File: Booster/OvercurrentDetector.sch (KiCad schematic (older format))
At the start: 35 parts, among them U202 LM339, U501 LM338, U502 LM358, U503 NE555

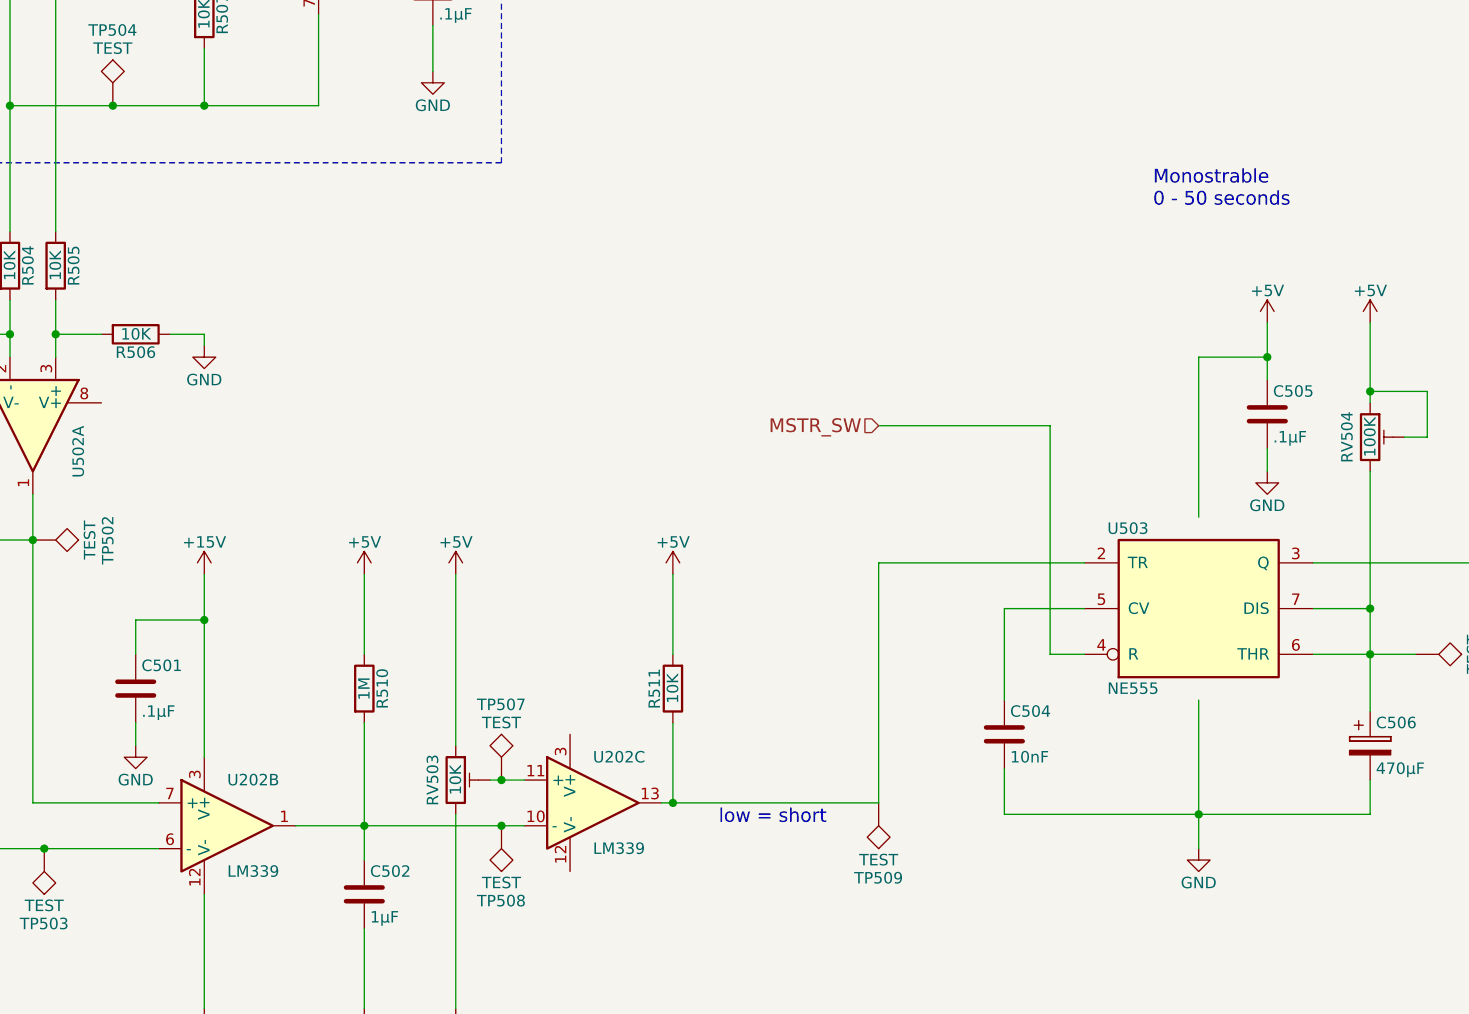
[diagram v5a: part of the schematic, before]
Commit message: Pulse detector circuit included.
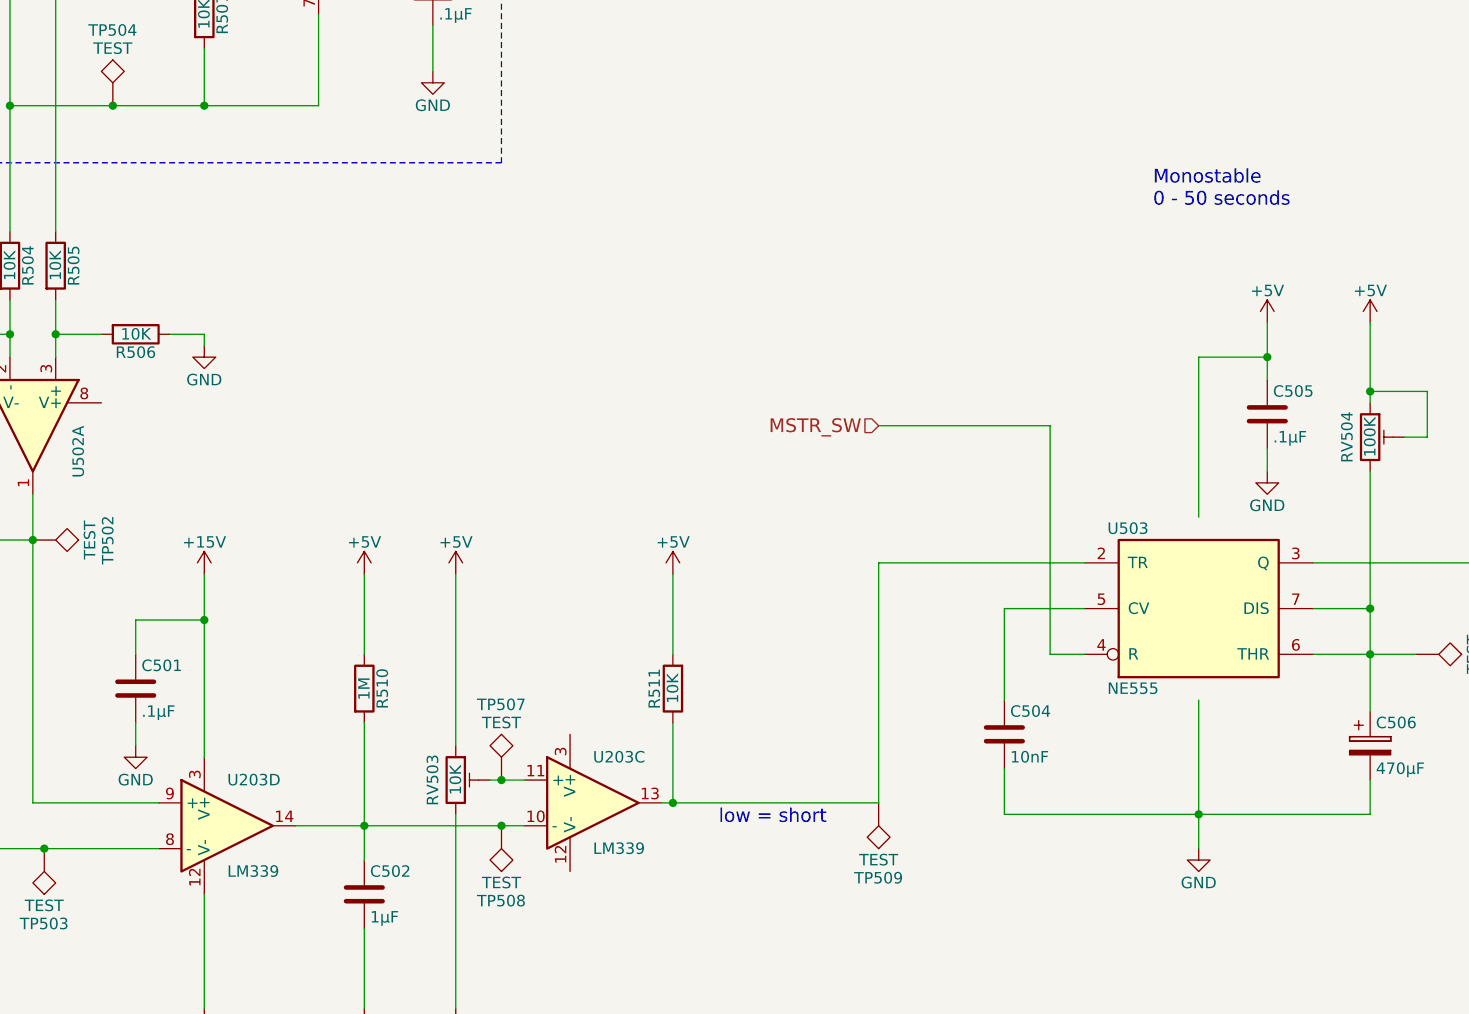
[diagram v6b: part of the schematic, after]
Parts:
- renumbered U202 to U203
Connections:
- net at R501.1, R502.2, TP503.1: now also U203.8 (-); no longer U203.6 (-)
- net at R503.2, TP502.1, U502.1: now also U203.9 (+); no longer U203.7 (+)
- net at C502.1, R510.2, TP508.1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: now also U203.14; no longer U203.1
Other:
- note added: "Monostable\n0 - 50 seconds"
- note removed: "Monostrable\n0 - 50 seconds"
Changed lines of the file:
@@
 $EndComp
 $Comp
-L GND #PWR016
+L GND #PWR501
 U 1 1 59ECCA64
 P 2500 7100
-F 0 "#PWR016" H 2500 6850 50  0001 C CNN
+F 0 "#PWR501" H 2500 6850 50  0001 C CNN
 F 1 "GND" H 2500 6950 50  0000 C CNN
 F 2 "" H 2500 7100 50  0000 C CNN
@@
 $EndComp
 $Comp
-L GND #PWR017
+L GND #PWR508
 U 1 1 5A073D4C
 P 4050 2150
-F 0 "#PWR017" H 4050 1900 50  0001 C CNN
+F 0 "#PWR508" H 4050 1900 50  0001 C CNN
 F 1 "GND" H 4050 2000 50  0000 C CNN
 F 2 "" H 4050 2150 50  0000 C CNN
@@
 $EndComp
 $Comp
-L GND #PWR018
+L GND #PWR512
 U 1 1 5A074775
 P 4900 2750
-F 0 "#PWR018" H 4900 2500 50  0001 C CNN
+F 0 "#PWR512" H 4900 2500 50  0001 C CNN
 F 1 "GND" H 4900 2600 50  0000 C CNN
 F 2 "" H 4900 2750 50  0000 C CNN
@@
 $EndComp
 $Comp
-L GND #PWR019
+L GND #PWR505
 U 1 1 5A076EC5
 P 3900 3950
-F 0 "#PWR019" H 3900 3700 50  0001 C CNN
+F 0 "#PWR505" H 3900 3700 50  0001 C CNN
 F 1 "GND" H 3900 3800 50  0000 C CNN
 F 2 "" H 3900 3950 50  0000 C CNN
@@
 $EndComp
 $Comp
-L +5V #PWR020
+L +5V #PWR503
 U 1 1 5A081F18
 P 2650 5450
-F 0 "#PWR020" H 2650 5300 50  0001 C CNN
+F 0 "#PWR503" H 2650 5300 50  0001 C CNN
 F 1 "+5V" H 2650 5590 50  0000 C CNN
 F 2 "" H 2650 5450 50  0000 C CNN
@@
 $EndComp
 $Comp
-L LM339 U202
-U 2 1 5A08213B
+L LM339 U203
+U 4 1 5A08213B
 P 4000 6050
-F 0 "U202" H 4000 6250 50  0000 L CNN
+F 0 "U203" H 4000 6250 50  0000 L CNN
 F 1 "LM339" H 4000 5850 50  0000 L CNN
 F 2 "" H 3950 6150 50  0000 C CNN
 F 3 "" H 4050 6250 50  0000 C CNN
-	2    4000 6050
+	4    4000 6050
 	1    0    0    -1
 $EndComp
@@
 $EndComp
 $Comp
-L LM339 U202
+L LM339 U203
 U 3 1 5A088F76
 P 5600 5950
-F 0 "U202" H 5600 6150 50  0000 L CNN
+F 0 "U203" H 5600 6150 50  0000 L CNN
 F 1 "LM339" H 5600 5750 50  0000 L CNN
 F 2 "" H 5550 6050 50  0000 C CNN
@@
 $EndComp
 $Comp
-L GND #PWR021
+L GND #PWR504
 U 1 1 5A092416
 P 3600 5700
-F 0 "#PWR021" H 3600 5450 50  0001 C CNN
+F 0 "#PWR504" H 3600 5450 50  0001 C CNN
 F 1 "GND" H 3600 5550 50  0000 C CNN
 F 2 "" H 3600 5700 50  0000 C CNN
@@
 $EndComp
 $Comp
-L +5V #PWR022
+L +5V #PWR509
 U 1 1 5A092870
 P 4600 4950
-F 0 "#PWR022" H 4600 4800 50  0001 C CNN
+F 0 "#PWR509" H 4600 4800 50  0001 C CNN
 F 1 "+5V" H 4600 5090 50  0000 C CNN
 F 2 "" H 4600 4950 50  0000 C CNN
@@
 $EndComp
 $Comp
-L +5V #PWR023
+L +5V #PWR513
 U 1 1 5A092928
 P 5000 4950
-F 0 "#PWR023" H 5000 4800 50  0001 C CNN
+F 0 "#PWR513" H 5000 4800 50  0001 C CNN
 F 1 "+5V" H 5000 5090 50  0000 C CNN
 F 2 "" H 5000 4950 50  0000 C CNN
@@
 $EndComp
 $Comp
-L GND #PWR024
+L GND #PWR507
 U 1 1 5A0931C8
 P 3900 6850
-F 0 "#PWR024" H 3900 6600 50  0001 C CNN
+F 0 "#PWR507" H 3900 6600 50  0001 C CNN
 F 1 "GND" H 3900 6700 50  0000 C CNN
 F 2 "" H 3900 6850 50  0000 C CNN
@@
 $EndComp
 $Comp
-L GND #PWR025
+L GND #PWR510
 U 1 1 5A093221
 P 4600 6850
-F 0 "#PWR025" H 4600 6600 50  0001 C CNN
+F 0 "#PWR510" H 4600 6600 50  0001 C CNN
 F 1 "GND" H 4600 6700 50  0000 C CNN
 F 2 "" H 4600 6850 50  0000 C CNN
@@
 $EndComp
 $Comp
-L GND #PWR026
+L GND #PWR514
 U 1 1 5A09327A
 P 5000 6850
-F 0 "#PWR026" H 5000 6600 50  0001 C CNN
+F 0 "#PWR514" H 5000 6600 50  0001 C CNN
 F 1 "GND" H 5000 6700 50  0000 C CNN
 F 2 "" H 5000 6850 50  0000 C CNN
@@
 $EndComp
 $Comp
-L +15V #PWR027
+L +15V #PWR502
 U 1 1 5A093E23
 P 2600 1200
-F 0 "#PWR027" H 2600 1050 50  0001 C CNN
+F 0 "#PWR502" H 2600 1050 50  0001 C CNN
 F 1 "+15V" H 2600 1340 50  0000 C CNN
 F 2 "" H 2600 1200 50  0000 C CNN
@@
 $EndComp
 $Comp
-L +15V #PWR028
+L +15V #PWR506
 U 1 1 5A094178
 P 3900 4950
-F 0 "#PWR028" H 3900 4800 50  0001 C CNN
+F 0 "#PWR506" H 3900 4800 50  0001 C CNN
 F 1 "+15V" H 3900 5090 50  0000 C CNN
 F 2 "" H 3900 4950 50  0000 C CNN
@@
 $EndComp
 $Comp
-L +15V #PWR029
+L +15V #PWR511
 U 1 1 5A0943E3
 P 4900 1850
-F 0 "#PWR029" H 4900 1700 50  0001 C CNN
+F 0 "#PWR511" H 4900 1700 50  0001 C CNN
 F 1 "+15V" H 4900 1990 50  0000 C CNN
 F 2 "" H 4900 1850 50  0000 C CNN
@@
 $EndComp
 $Comp
-L +5V #PWR030
+L +5V #PWR515
 U 1 1 5A36B721
 P 5950 4950
-F 0 "#PWR030" H 5950 4800 50  0001 C CNN
+F 0 "#PWR515" H 5950 4800 50  0001 C CNN
 F 1 "+5V" H 5950 5090 50  0000 C CNN
 F 2 "" H 5950 4950 50  0000 C CNN
@@
 $EndComp
 $Comp
-L +5V #PWR031
+L +5V #PWR517
 U 1 1 5A36C438
 P 8550 3850
-F 0 "#PWR031" H 8550 3700 50  0001 C CNN
+F 0 "#PWR517" H 8550 3700 50  0001 C CNN
 F 1 "+5V" H 8550 3990 50  0000 C CNN
 F 2 "" H 8550 3850 50  0000 C CNN
@@
 $EndComp
 $Comp
-L GND #PWR032
+L GND #PWR518
 U 1 1 5A36CF5F
 P 8550 4500
-F 0 "#PWR032" H 8550 4250 50  0001 C CNN
+F 0 "#PWR518" H 8550 4250 50  0001 C CNN
 F 1 "GND" H 8550 4350 50  0000 C CNN
 F 2 "" H 8550 4500 50  0000 C CNN
@@
 $EndComp
 $Comp
-L +5V #PWR033
+L +5V #PWR519
 U 1 1 5A36D304
 P 9000 3850
-F 0 "#PWR033" H 9000 3700 50  0001 C CNN
+F 0 "#PWR519" H 9000 3700 50  0001 C CNN
 F 1 "+5V" H 9000 3990 50  0000 C CNN
 F 2 "" H 9000 3850 50  0000 C CNN
@@
 Connection ~ 8250 6000
 $Comp
-L GND #PWR034
+L GND #PWR516
 U 1 1 5A36DC1B
 P 8250 6150
-F 0 "#PWR034" H 8250 5900 50  0001 C CNN
+F 0 "#PWR516" H 8250 5900 50  0001 C CNN
 F 1 "GND" H 8250 6000 50  0000 C CNN
 F 2 "" H 8250 6150 50  0000 C CNN
@@
 	9000 6000 9000 5850
 Text Notes 8050 3350 0    60   ~ 0
-Monostrable\n0 - 50 seconds
+Monostable\n0 - 50 seconds
 $Comp
 L TEST TP509

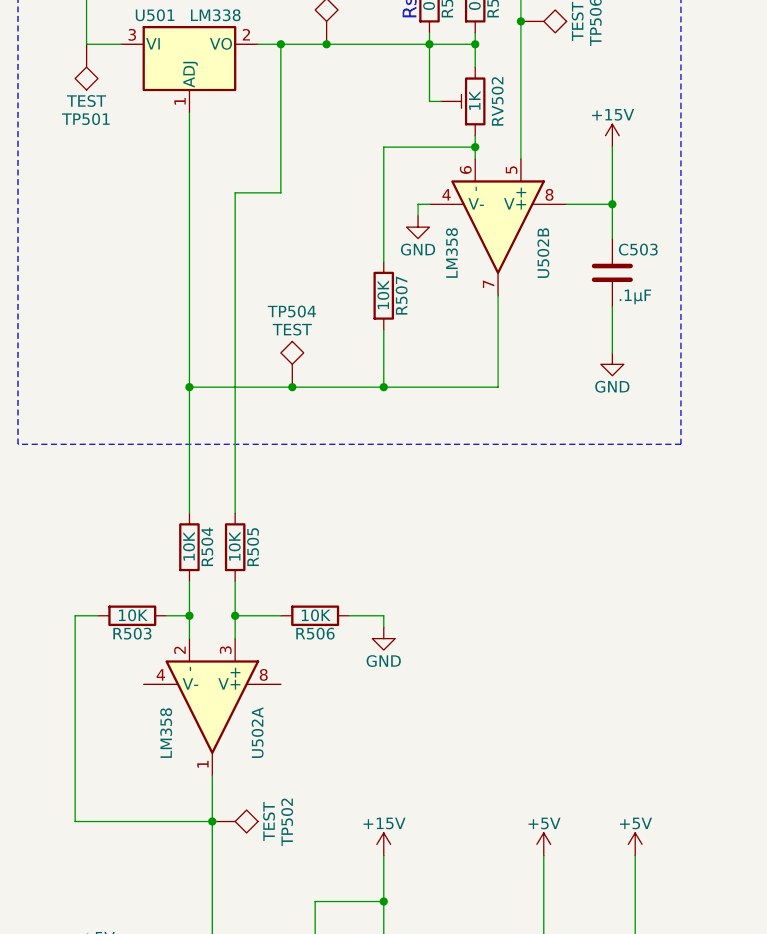
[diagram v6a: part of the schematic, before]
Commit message: Various adjustments based on breadboard prototype.
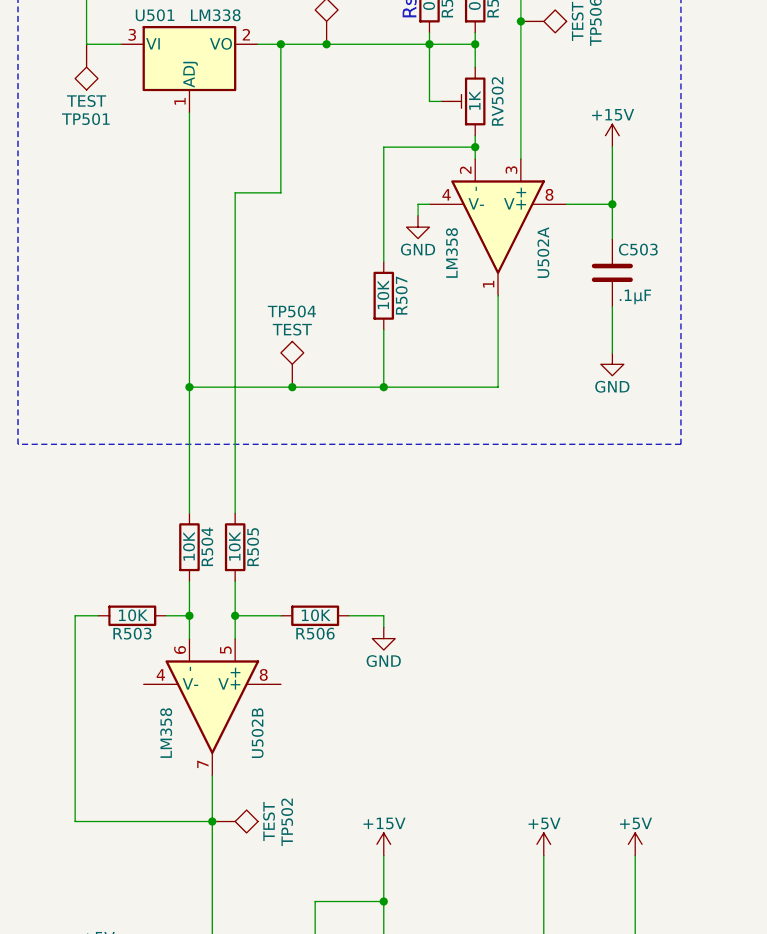
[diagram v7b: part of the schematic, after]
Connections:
- net VCC_DRIVER: now also U502.3 (+); no longer U502.5 (+)
- net at R504.1, R507.2, TP504.1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: now also U502.1; no longer U502.7
- net at R507.1, RV502.1: now also U502.2 (-); no longer U502.6 (-)
- net at R503.2, TP502.1, U203.9 (+): now also U502.7; no longer U502.1
- net at R503.1, R504.2: now also U502.6 (-); no longer U502.2 (-)
- net at R505.2, R506.2: now also U502.5 (+); no longer U502.3 (+)
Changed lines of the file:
@@
 $EndComp
 $Comp
-L GND #PWR501
+L GND #PWR019
 U 1 1 59ECCA64
 P 2500 7100
-F 0 "#PWR501" H 2500 6850 50  0001 C CNN
+F 0 "#PWR019" H 2500 6850 50  0001 C CNN
 F 1 "GND" H 2500 6950 50  0000 C CNN
 F 2 "" H 2500 7100 50  0000 C CNN
@@
 $Comp
 L LM358 U502
-U 2 1 5A071933
+U 1 1 5A071933
 P 4400 2200
 F 0 "U502" H 4400 2400 50  0000 L CNN
@@
 F 2 "" H 4400 2200 50  0001 C CNN
 F 3 "" H 4400 2200 50  0001 C CNN
-	2    4400 2200
+	1    4400 2200
 	0    1    1    0
 $EndComp
@@
 $EndComp
 $Comp
-L GND #PWR508
+L GND #PWR020
 U 1 1 5A073D4C
 P 4050 2150
-F 0 "#PWR508" H 4050 1900 50  0001 C CNN
+F 0 "#PWR020" H 4050 1900 50  0001 C CNN
 F 1 "GND" H 4050 2000 50  0000 C CNN
 F 2 "" H 4050 2150 50  0000 C CNN
@@
 $EndComp
 $Comp
-L GND #PWR512
+L GND #PWR021
 U 1 1 5A074775
 P 4900 2750
-F 0 "#PWR512" H 4900 2500 50  0001 C CNN
+F 0 "#PWR021" H 4900 2500 50  0001 C CNN
 F 1 "GND" H 4900 2600 50  0000 C CNN
 F 2 "" H 4900 2750 50  0000 C CNN
@@
 $Comp
 L LM358 U502
-U 1 1 5A076258
+U 2 1 5A076258
 P 3150 4300
 F 0 "U502" H 3150 4500 50  0000 L CNN
@@
 F 2 "" H 3150 4300 50  0001 C CNN
 F 3 "" H 3150 4300 50  0001 C CNN
-	1    3150 4300
+	2    3150 4300
 	0    1    1    0
 $EndComp
@@
 $EndComp
 $Comp
-L GND #PWR505
+L GND #PWR022
 U 1 1 5A076EC5
 P 3900 3950
-F 0 "#PWR505" H 3900 3700 50  0001 C CNN
+F 0 "#PWR022" H 3900 3700 50  0001 C CNN
 F 1 "GND" H 3900 3800 50  0000 C CNN
 F 2 "" H 3900 3950 50  0000 C CNN
@@
 $EndComp
 $Comp
-L +5V #PWR503
+L +5V #PWR023
 U 1 1 5A081F18
 P 2650 5450
-F 0 "#PWR503" H 2650 5300 50  0001 C CNN
+F 0 "#PWR023" H 2650 5300 50  0001 C CNN
 F 1 "+5V" H 2650 5590 50  0000 C CNN
 F 2 "" H 2650 5450 50  0000 C CNN
@@
 $EndComp
 $Comp
-L GND #PWR504
+L GND #PWR024
 U 1 1 5A092416
 P 3600 5700
-F 0 "#PWR504" H 3600 5450 50  0001 C CNN
+F 0 "#PWR024" H 3600 5450 50  0001 C CNN
 F 1 "GND" H 3600 5550 50  0000 C CNN
 F 2 "" H 3600 5700 50  0000 C CNN
@@
 $EndComp
 $Comp
-L +5V #PWR509
+L +5V #PWR025
 U 1 1 5A092870
 P 4600 4950
-F 0 "#PWR509" H 4600 4800 50  0001 C CNN
+F 0 "#PWR025" H 4600 4800 50  0001 C CNN
 F 1 "+5V" H 4600 5090 50  0000 C CNN
 F 2 "" H 4600 4950 50  0000 C CNN
@@
 $EndComp
 $Comp
-L +5V #PWR513
+L +5V #PWR026
 U 1 1 5A092928
 P 5000 4950
-F 0 "#PWR513" H 5000 4800 50  0001 C CNN
+F 0 "#PWR026" H 5000 4800 50  0001 C CNN
 F 1 "+5V" H 5000 5090 50  0000 C CNN
 F 2 "" H 5000 4950 50  0000 C CNN
@@
 $EndComp
 $Comp
-L GND #PWR507
+L GND #PWR027
 U 1 1 5A0931C8
 P 3900 6850
-F 0 "#PWR507" H 3900 6600 50  0001 C CNN
+F 0 "#PWR027" H 3900 6600 50  0001 C CNN
 F 1 "GND" H 3900 6700 50  0000 C CNN
 F 2 "" H 3900 6850 50  0000 C CNN
@@
 $EndComp
 $Comp
-L GND #PWR510
+L GND #PWR028
 U 1 1 5A093221
 P 4600 6850
-F 0 "#PWR510" H 4600 6600 50  0001 C CNN
+F 0 "#PWR028" H 4600 6600 50  0001 C CNN
 F 1 "GND" H 4600 6700 50  0000 C CNN
 F 2 "" H 4600 6850 50  0000 C CNN
@@
 $EndComp
 $Comp
-L GND #PWR514
+L GND #PWR029
 U 1 1 5A09327A
 P 5000 6850
-F 0 "#PWR514" H 5000 6600 50  0001 C CNN
+F 0 "#PWR029" H 5000 6600 50  0001 C CNN
 F 1 "GND" H 5000 6700 50  0000 C CNN
 F 2 "" H 5000 6850 50  0000 C CNN
@@
 $EndComp
 $Comp
-L +15V #PWR502
+L +15V #PWR030
 U 1 1 5A093E23
 P 2600 1200
-F 0 "#PWR502" H 2600 1050 50  0001 C CNN
+F 0 "#PWR030" H 2600 1050 50  0001 C CNN
 F 1 "+15V" H 2600 1340 50  0000 C CNN
 F 2 "" H 2600 1200 50  0000 C CNN
@@
 $EndComp
 $Comp
-L +15V #PWR506
+L +15V #PWR031
 U 1 1 5A094178
 P 3900 4950
-F 0 "#PWR506" H 3900 4800 50  0001 C CNN
+F 0 "#PWR031" H 3900 4800 50  0001 C CNN
 F 1 "+15V" H 3900 5090 50  0000 C CNN
 F 2 "" H 3900 4950 50  0000 C CNN
@@
 $EndComp
 $Comp
-L +15V #PWR511
+L +15V #PWR032
 U 1 1 5A0943E3
 P 4900 1850
-F 0 "#PWR511" H 4900 1700 50  0001 C CNN
+F 0 "#PWR032" H 4900 1700 50  0001 C CNN
 F 1 "+15V" H 4900 1990 50  0000 C CNN
 F 2 "" H 4900 1850 50  0000 C CNN
@@
 $EndComp
 $Comp
-L +5V #PWR515
+L +5V #PWR033
 U 1 1 5A36B721
 P 5950 4950
-F 0 "#PWR515" H 5950 4800 50  0001 C CNN
+F 0 "#PWR033" H 5950 4800 50  0001 C CNN
 F 1 "+5V" H 5950 5090 50  0000 C CNN
 F 2 "" H 5950 4950 50  0000 C CNN
@@
 $EndComp
 $Comp
-L +5V #PWR517
+L +5V #PWR034
 U 1 1 5A36C438
 P 8550 3850
-F 0 "#PWR517" H 8550 3700 50  0001 C CNN
+F 0 "#PWR034" H 8550 3700 50  0001 C CNN
 F 1 "+5V" H 8550 3990 50  0000 C CNN
 F 2 "" H 8550 3850 50  0000 C CNN
@@
 $EndComp
 $Comp
-L GND #PWR518
+L GND #PWR035
 U 1 1 5A36CF5F
 P 8550 4500
-F 0 "#PWR518" H 8550 4250 50  0001 C CNN
+F 0 "#PWR035" H 8550 4250 50  0001 C CNN
 F 1 "GND" H 8550 4350 50  0000 C CNN
 F 2 "" H 8550 4500 50  0000 C CNN
@@
 $EndComp
 $Comp
-L +5V #PWR519
+L +5V #PWR036
 U 1 1 5A36D304
 P 9000 3850
-F 0 "#PWR519" H 9000 3700 50  0001 C CNN
+F 0 "#PWR036" H 9000 3700 50  0001 C CNN
 F 1 "+5V" H 9000 3990 50  0000 C CNN
 F 2 "" H 9000 3850 50  0000 C CNN
@@
 Connection ~ 8250 6000
 $Comp
-L GND #PWR516
+L GND #PWR037
 U 1 1 5A36DC1B
 P 8250 6150
-F 0 "#PWR516" H 8250 5900 50  0001 C CNN
+F 0 "#PWR037" H 8250 5900 50  0001 C CNN
 F 1 "GND" H 8250 6000 50  0000 C CNN
 F 2 "" H 8250 6150 50  0000 C CNN
